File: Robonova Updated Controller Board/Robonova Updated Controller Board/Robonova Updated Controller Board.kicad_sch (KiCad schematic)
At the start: 44 parts

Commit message: cleanup and start of schematic
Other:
- note added: "Connectors and power led"
- note added: "I2C Address selector"
- note added: "Output pins servo's"
- note added: "PCA9685 controller"
- note added: "Piezo speaker"
- note added: "Reverse voltage protection"
- note added: "Servo's"
- note added: "adress = 1 + A1 +A0 + RW"
- note removed: "1 + A1 +A0 + RW"
- note removed: "I2C Address ="
- note removed: "Reverse voltage"
- note removed: "protection"
- moved on the sheet: C?, J?, JL?, JP?, JR?, JSensor?, LED?, LS?, Q?, R?, R?A, R?B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

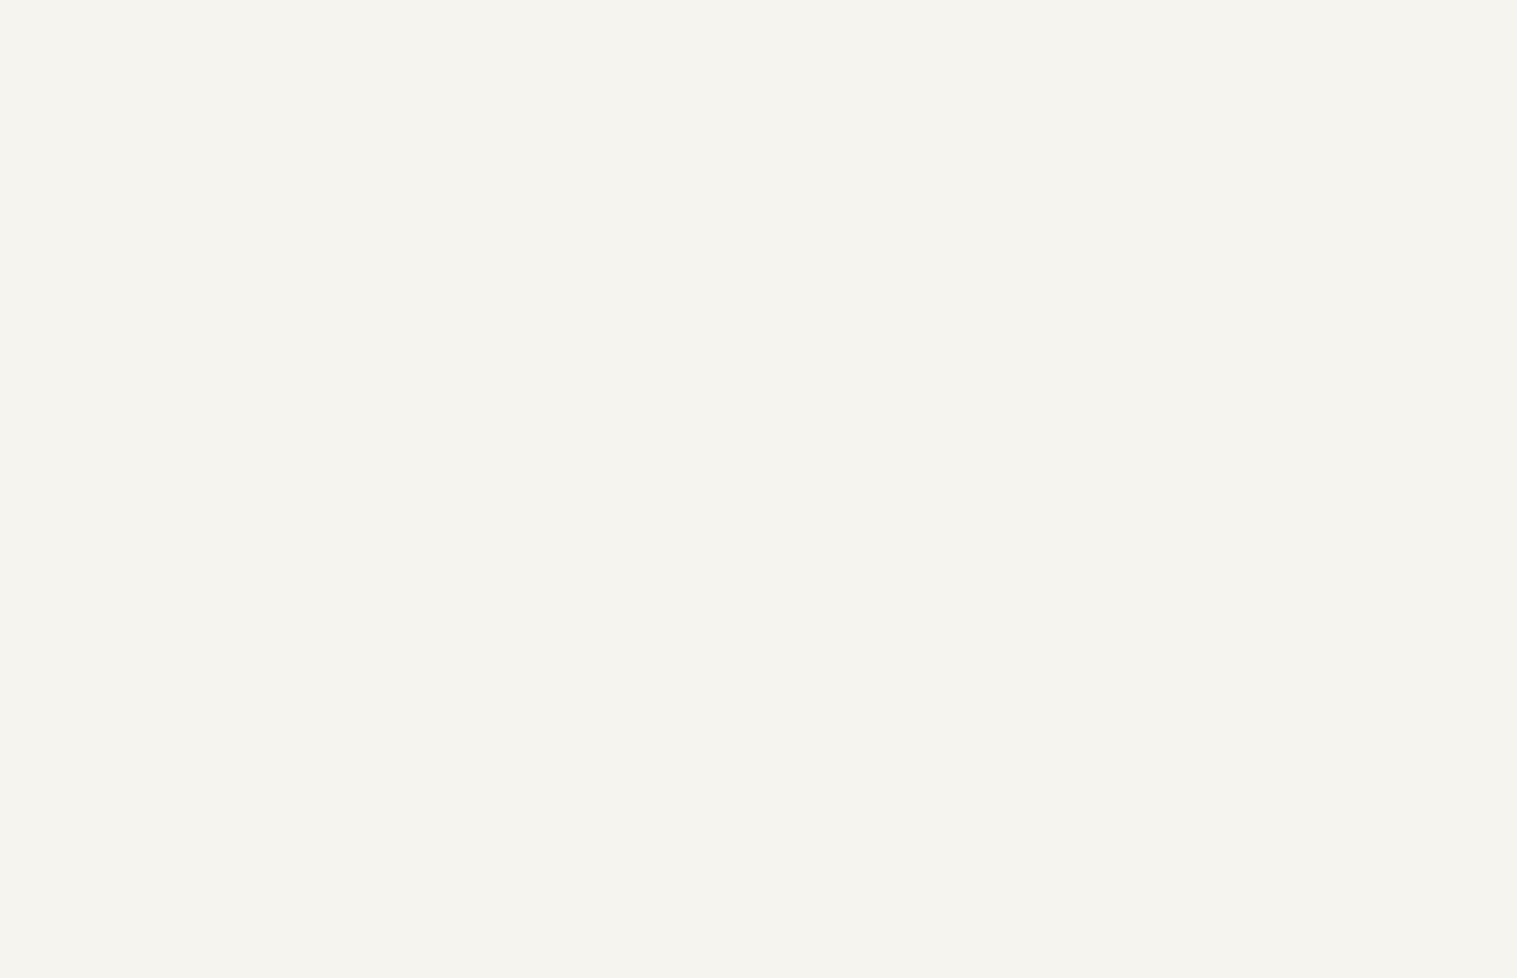
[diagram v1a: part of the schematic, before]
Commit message: started gyroscope schematic
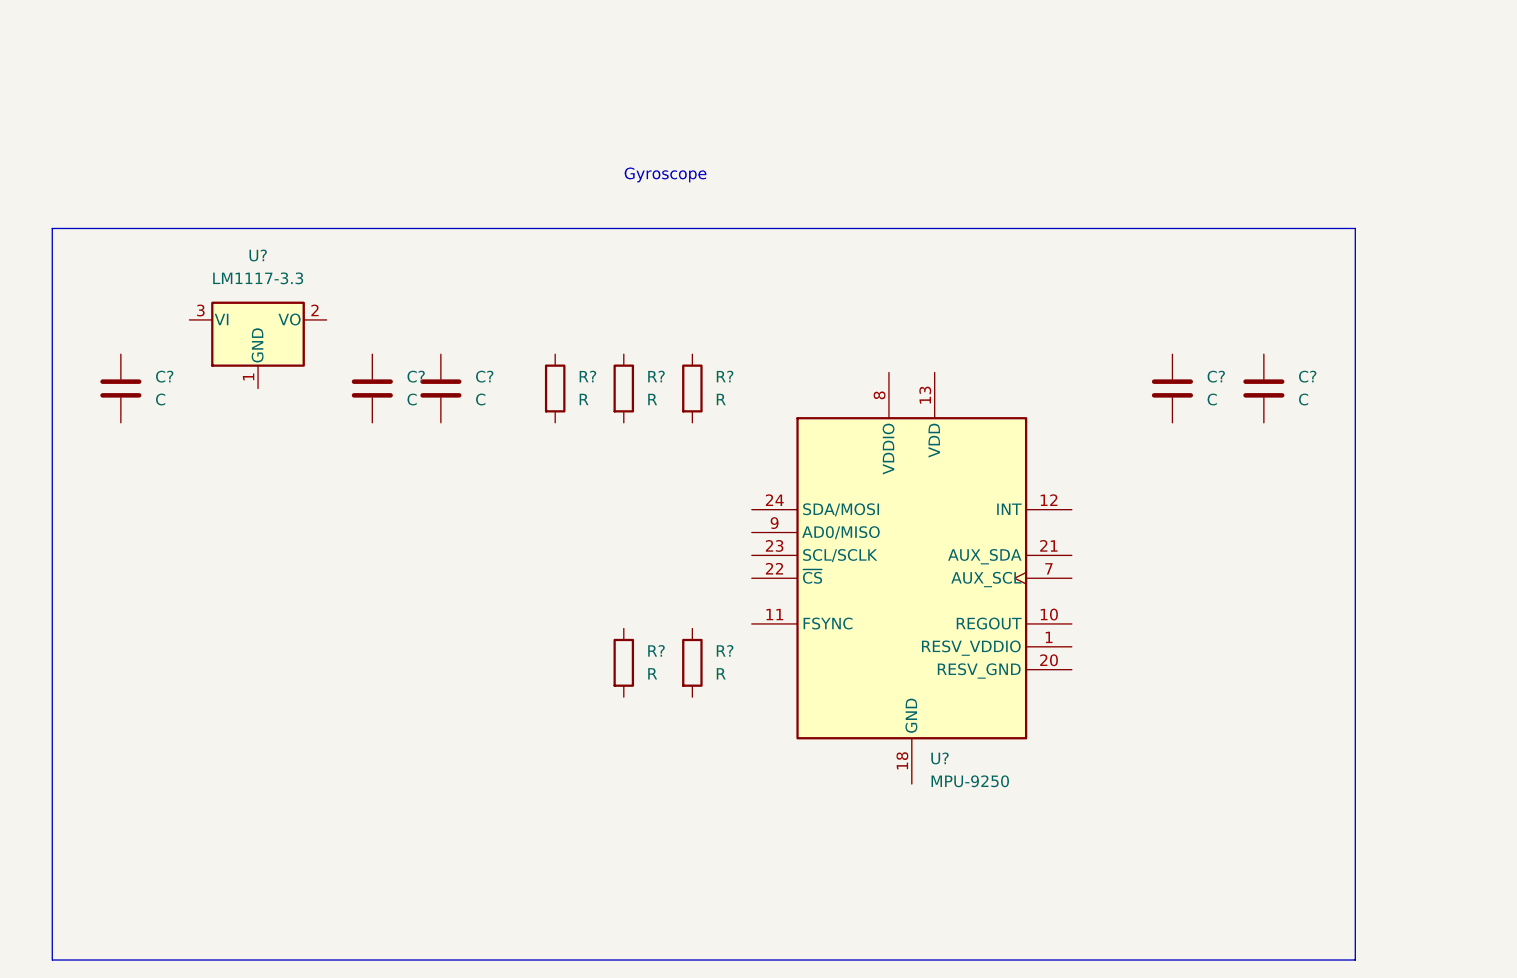
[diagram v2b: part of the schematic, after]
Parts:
- added C? (x5): C, symbol Device:C
- added R? (x5): R, symbol Device:R
- added U?: LM1117-3.3, symbol Regulator_Linear:LM1117-3.3
- added U?: MPU-9250, Sensor_Motion:InvenSense_QFN-24_3x3mm_P0.4mm, symbol Sensor_Motion:MPU-9250
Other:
- note added: "Gyroscope"

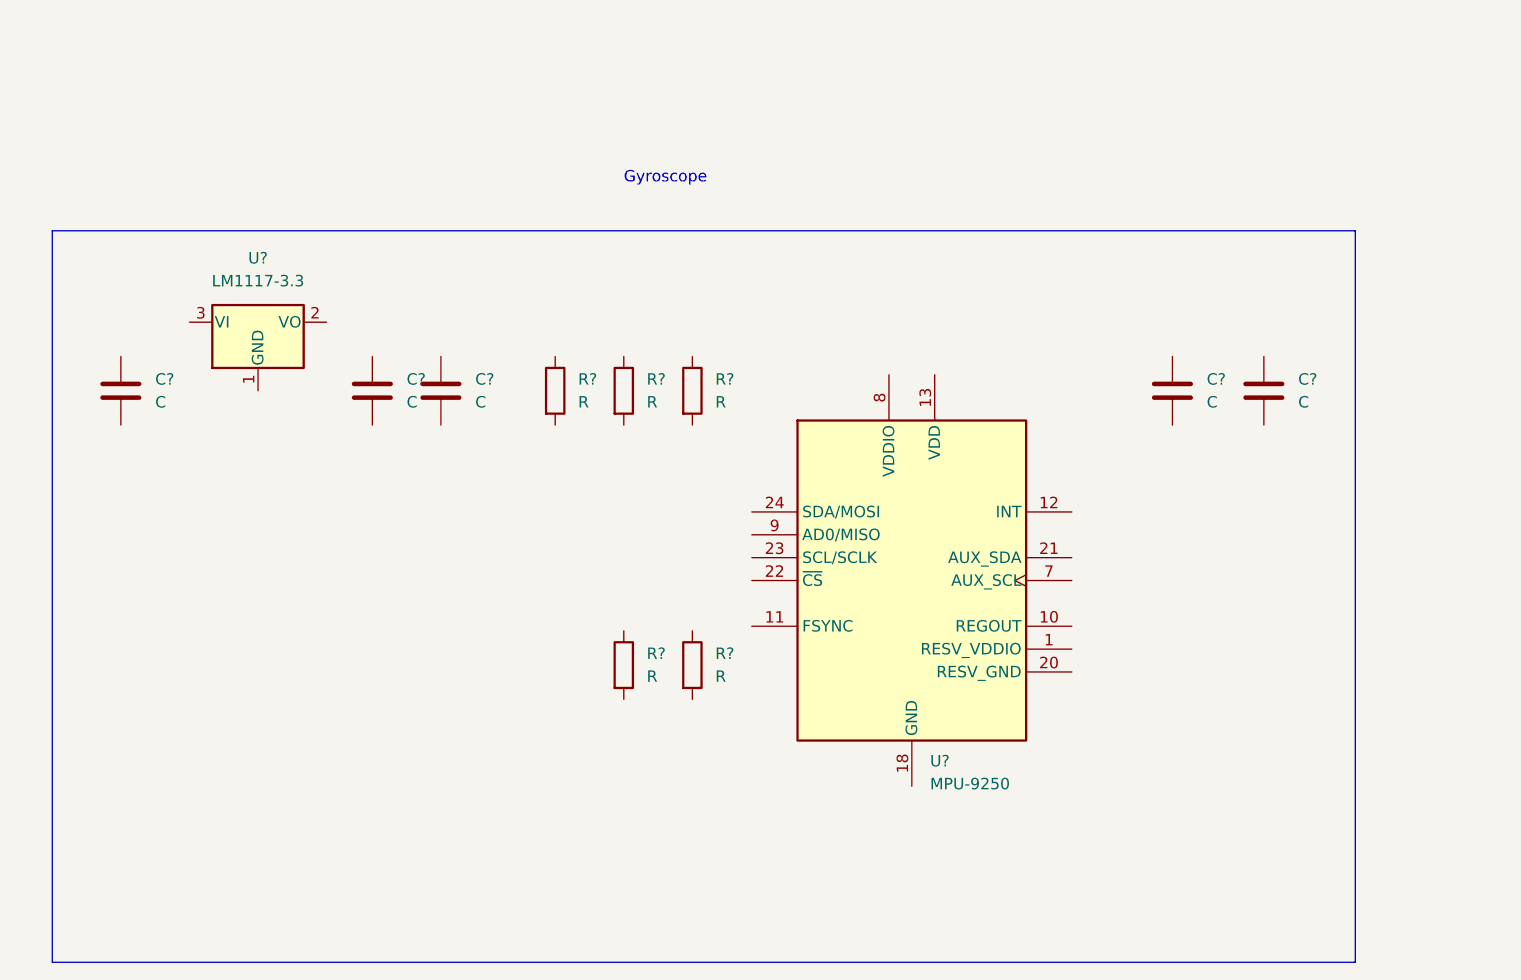
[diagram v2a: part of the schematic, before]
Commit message: finished imu schematic
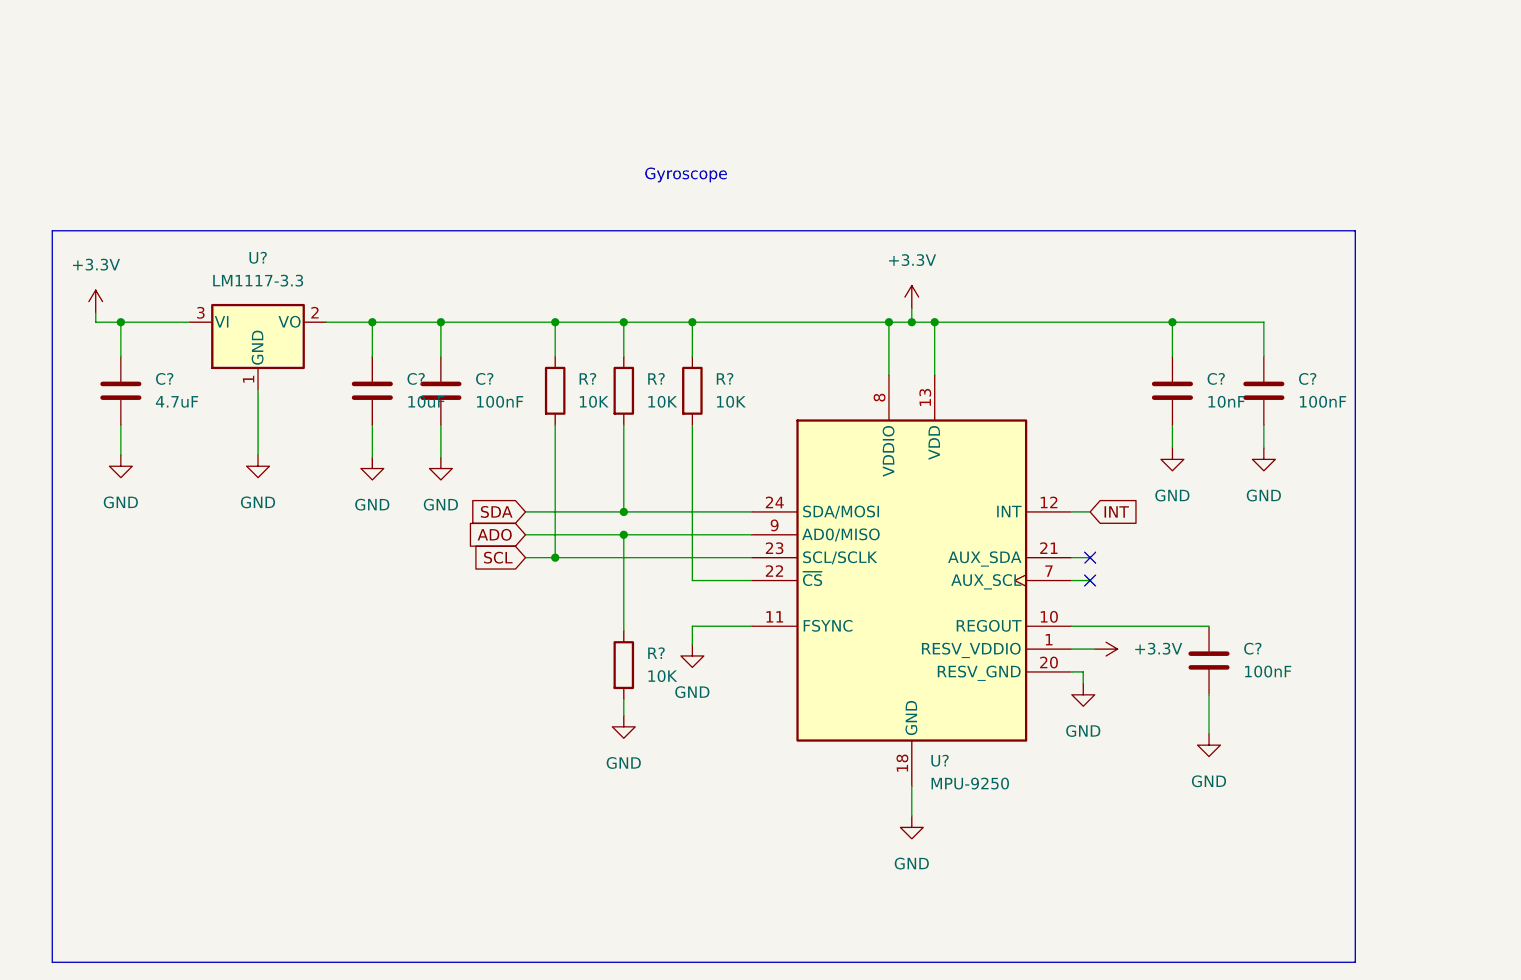
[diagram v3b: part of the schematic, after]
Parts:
- removed R?: R, symbol Device:R
- added C?: 100nF, symbol Device:C
- C? (x2): value C -> 100nF
- C?: value C -> 10uF
- C?: value C -> 4.7uF
- C?: value C -> 10nF
- R? (x4): value R -> 10K
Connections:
- net GND: now also C?.2, C?.2, C?.2, C?.2, C?.2, R?.2, U?.1 (GND), U?.11 (FSYNC), U?.18 (GND), U?.20 (RESV_GND), C?.2
- net SCL: now also R?.2, U?.23 (SCL/SCLK)
- net SDA: now also R?.2, U?.24 (SDA/MOSI)
- net +3.3V: now reaches R?.1
- net +3.3V: now also C?.1, C?.1, C?.1, C?.1, C?.1, R?.1, R?.1, U?.1 (RESV_VDDIO), U?.13 (VDD), U?.2 (VO), U?.3 (VI), U?.8 (VDDIO)
- net ADO: now reaches R?.1
- net ADO: now also U?.9 (AD0/MISO)
- net at U?.10 (REGOUT): now also C?.1
- net INT: now reaches U?.12 (INT)
- net at U?.22 (~{CS}): now also R?.2
- no-connect marks 4 -> 6

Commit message: started overdischarge protection circuit design
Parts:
- removed C? (x3): 100nF, symbol Device:C
- removed C?: 10uF, symbol Device:C
- removed C?: 4.7uF, symbol Device:C
- removed C?: 10nF, symbol Device:C
- removed R? (x4): 10K, symbol Device:R
- removed U?: LM1117-3.3, symbol Regulator_Linear:LM1117-3.3
- removed U?: MPU-9250, Sensor_Motion:InvenSense_QFN-24_3x3mm_P0.4mm, symbol Sensor_Motion:MPU-9250
- added C? (x2): 0.1uF, Robonova Updated Controller Board:0603, symbol Robonova Updated Controller Board-eagle-import:0.1UF-0603-25V-5%
- added C? (x2): 1.0uF, Robonova Updated Controller Board:0603, symbol Robonova Updated Controller Board-eagle-import:1.0UF-0603-16V-10%-X7R
- added D?: D_Zener, symbol Device:D_Zener
- added D?: RED, Robonova Updated Controller Board:LED-0603, symbol Robonova Updated Controller Board-eagle-import:LED-RED0603
- added JP?: AUX, Robonova Updated Controller Board:SMT-JUMPER_3_2-NC_TRACE_SILK, symbol Robonova Updated Controller Board-eagle-import:JUMPER-SMT_3_2-NC_TRACE_SILK
- added JP?: LED, Robonova Updated Controller Board:SMT-JUMPER_2_NC_TRACE_SILK, symbol Robonova Updated Controller Board-eagle-import:JUMPER-SMT_2_NC_TRACE_SILK
- added JP?: I2C PU, Robonova Updated Controller Board:SMT-JUMPER_3_2-NC_TRACE_SILK, symbol Robonova Updated Controller Board-eagle-import:JUMPER-SMT_3_2-NC_TRACE_SILK
- added JP?: ADR, Robonova Updated Controller Board:SMT-JUMPER_2_NO_SILK, symbol Robonova Updated Controller Board-eagle-import:JUMPER-SMT_2_NO_SILK
- added Q? (x4): 20V/0.2A/8MHz/1.2Ω/1Vth, Robonova Updated Controller Board:SOT-416FL, symbol Robonova Updated Controller Board-eagle-import:MOSFET-NCH-RE1C002UN
- added R?: 220, Robonova Updated Controller Board:0603, symbol Robonova Updated Controller Board-eagle-import:220OHM-0603-1/10W-1%
- added R? (x8): 2.2k, Robonova Updated Controller Board:0402-TIGHT, symbol Robonova Updated Controller Board-eagle-import:2.2KOHM-0402T-1/16W-1%
- added R? (x3): R, symbol Device:R
- added T?: TIP122, TO220, symbol TIP122:TIP122
- added TP?: 1.8V, Robonova Updated Controller Board:PAD.03X.03, symbol Robonova Updated Controller Board-eagle-import:TEST-POINT3
- added U?: TIP36C, SOT93, symbol TIP36C:TIP36C
- added U?: 9DoF IMU, Robonova Updated Controller Board:QFN24-3X3, symbol Robonova Updated Controller Board-eagle-import:ICM-20948
- added U?: 1.8V/100mA, Robonova Updated Controller Board:SC70, symbol Robonova Updated Controller Board-eagle-import:V_REG_SP6214-1.8V
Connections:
- net INT: now also U?.12 (INT)
- net VIN: now also C?.1, JP?.2, JP?.2, U?.1 (IN), U?.3 (EN)
- net GND renamed -BATT
- net -BATT: now also C?.2, C?.2, C?.2, C?.2, JP?.1, JP?.1, R?.1, T?.3, U?.18 (GND), U?.2 (GND), U?.20 (GND)
- new net: JP?.2, R?.1
- new net: D?.C, R?.2
- new net: JP?.3, R?.2 (x2)
- new net: R?.1, U?.B
- new net: R?.1, T?.1
- new net: D?.2 (A), R?.2, R?.2
- new net: JP?.1, R?.2 (x2)
- new net: R?.2, T?.2
- new net: C?.1, U?.10 (REGOUT)
- new net +BATT: D?.1 (K), U?.E
- new net 1.8V: C?.1, C?.1, D?.A, Q?.1 (G), Q?.1 (G), Q?.1 (G), Q?.1 (G), R?.2, R?.2, R?.2, R?.2, TP?.P$1 (1), U?.13 (VDD), U?.5 (OUT), U?.8 (VDDIO)
- new net 7.4V-8.4V: U?.C
- new net AD0/SDO: U?.9 (AD0/SDO)
- new net AD0/SDO_VIN: JP?.2
- new net AUX_CL: Q?.2 (S), R?.1, U?.7 (AUX_CL)
- new net AUX_CL_VIN: Q?.3 (D), R?.1
- new net AUX_DA: Q?.2 (S), R?.1, U?.21 (AUX_DA)
- new net AUX_DA_VIN: Q?.3 (D), R?.1
- new net FSYNC: U?.11 (FSYNC)
- new net SCL/SCLK: Q?.2 (S), R?.1, U?.23 (SCL/SCLK)
- new net SCL/SCLK_VIN: Q?.3 (D), R?.1
- new net SDA/SDI: Q?.2 (S), R?.1, U?.24 (SDA/SDI)
- new net SDA/SDI_VIN: Q?.3 (D), R?.1
- new net ~{CS}: U?.22 (~{CS})
- no-connect marks 6 -> 4
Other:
- note added: "ADR -> I2C Address ------------------- open -> 0x69 closed -> 0x68 *Closing AD0 precludes SPI"
- note added: "Adress selector"
- note added: "Cut to disable PWR LED"
- note added: "IMU"
- note added: "Overdischarge protection"
- note added: "Reverse voltage protection (not required?)"
- note added: "VIN 1.8V to 5.5V"
- note added: "esp32 wroom 1 dev board connector"
- note added: "level shifting and pull-up disconnects"
- note added: "voltage regulator"
- note removed: "Gyroscope"
- note removed: "Reverse voltage protection"
- moved on the sheet: C?, J?, JL?, JP?, JR?, JSensor?, LED?, LS?, Q?, R?, R?A, R?B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
